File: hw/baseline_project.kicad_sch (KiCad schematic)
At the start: 20 parts, among them J101 EXT_3V3, Q101 IRLD024PBF, SW101 UP, SW102 DOWN, SW103 LEFT, SW104 RIGHT, SW105 MODE, U101 EK-TM4C123GXL, U102 ESP8266-1, U103 Adafruit ST7735R

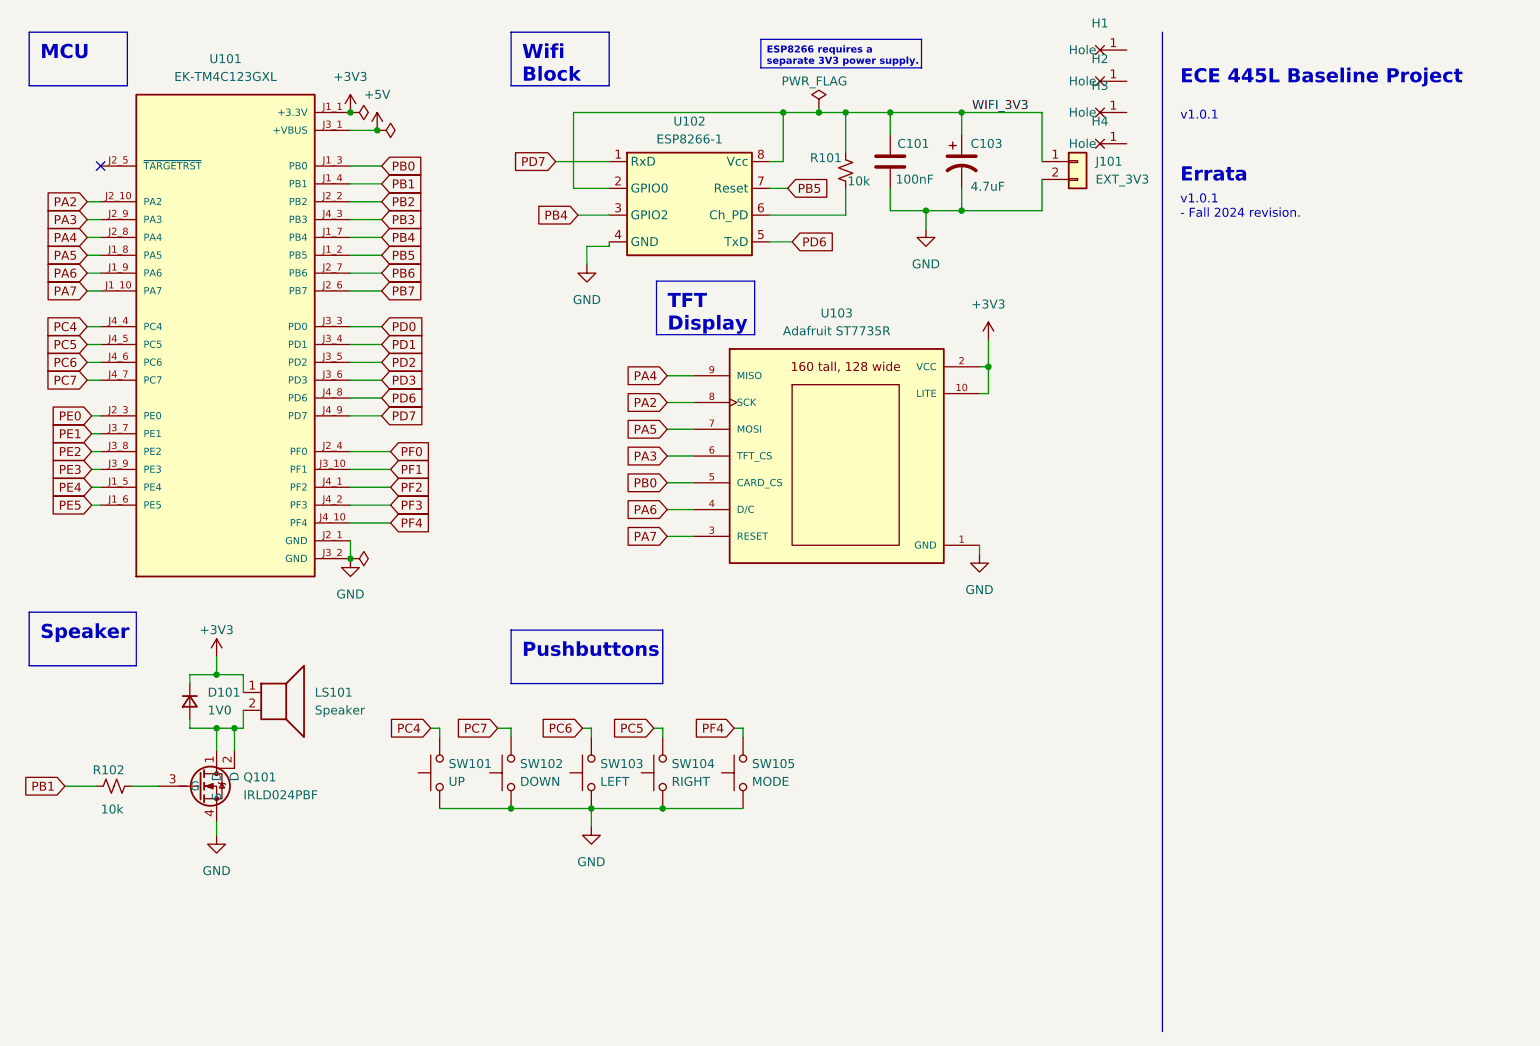
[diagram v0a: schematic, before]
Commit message: changed schematic
Updated schematic pins and layout to make sense with our design for lab3
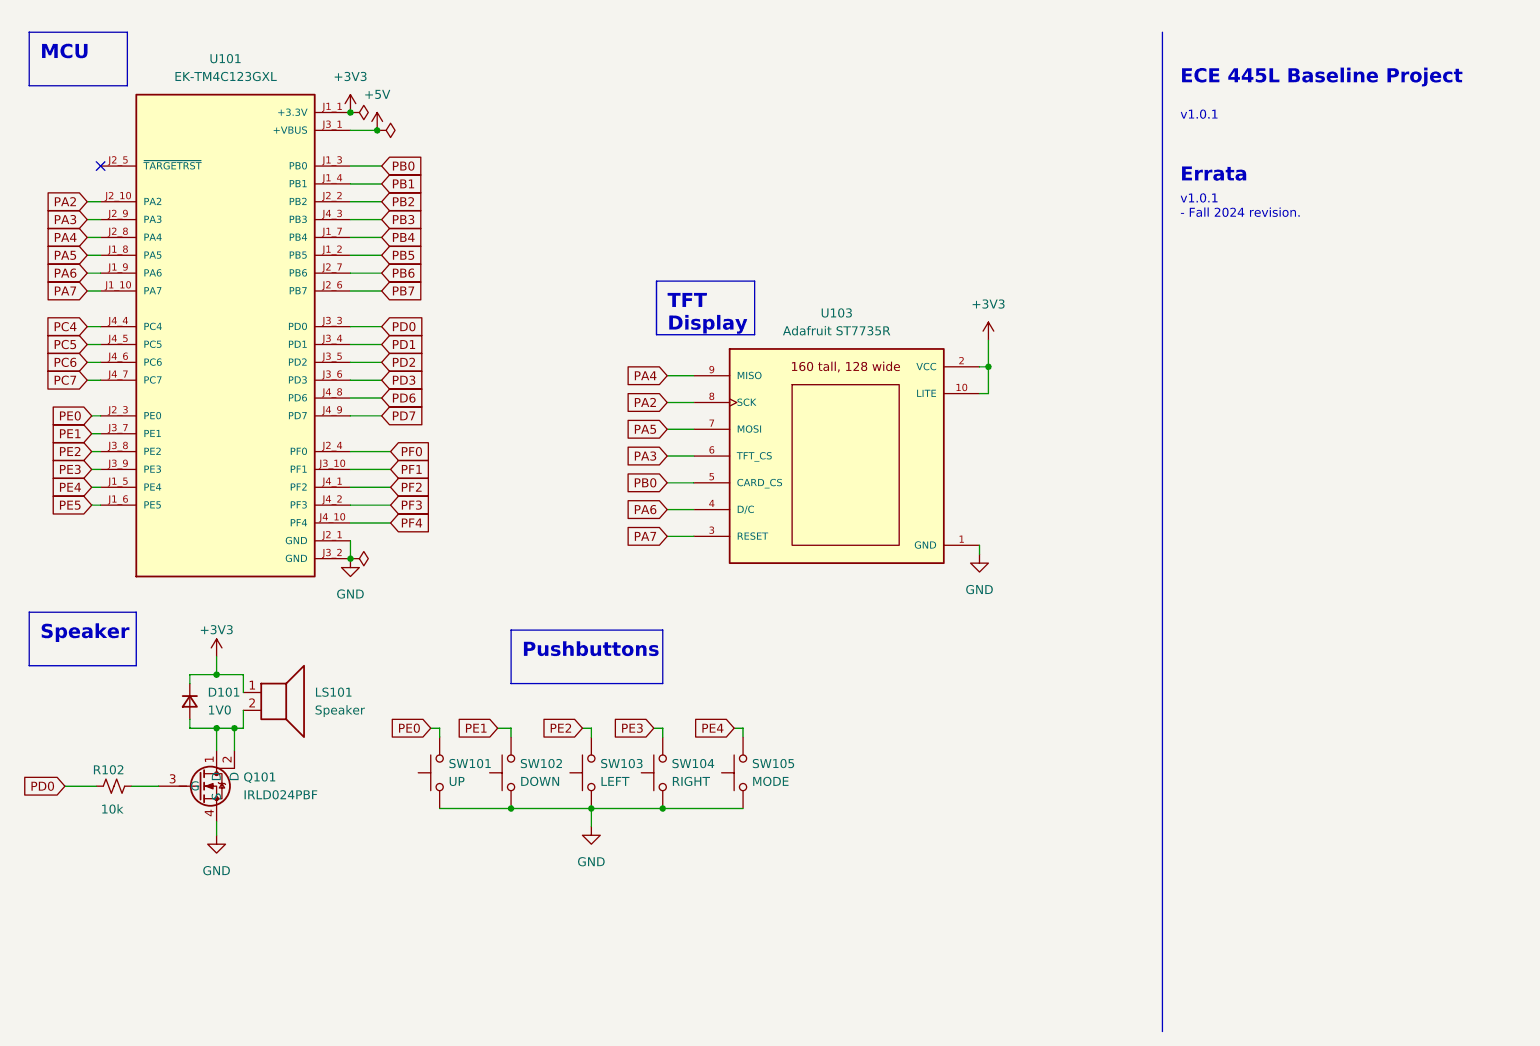
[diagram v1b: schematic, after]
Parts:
- removed C101: 100nF, ECE445L:C_Axial_200mil, symbol ECE445L:C
- removed C103: 4.7uF, ECE445L:CP_Radial_Tantal200mil, symbol ECE445L:C_Polarized
- removed H1, H2, H3, H4: ~, ECE445L:MountingHole_4_40, symbol ECE445L:MountingHole
- removed J101: EXT_3V3, Connector_Samtec_HPM_THT:Samtec_HPM-02-01-x-S_Straight_1x02_Pitch5.08mm, symbol Connector_Generic:Conn_01x02
- removed R101: 10k, ECE445L:R_Axial_DIN0204_L3.6mm_D1.6mm_P7.62mm_Horizontal, symbol ECE445L:R_0.125W
- removed U102: ESP8266-1, ECE445L:PinHeader_2x04_P2.54mm_Vertical, symbol ECE445L:ESP8266-1
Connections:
- net PB1: no longer R102.1
- net PC4: no longer SW101.2
- net PC5: no longer SW104.2
- net PC6: no longer SW103.2
- net PC7: no longer SW102.2
- net PD0: now also R102.1
- net PE0: now also SW101.2
- net PE1: now also SW102.2
- net PE2: now also SW103.2
- net PE3: now also SW104.2
- net PE4: now also SW105.2
- net PF4: no longer SW105.2

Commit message: new updates
added heartbeat back in (untested). Made an initial attempt to draw the background of the clock, probably won't work.
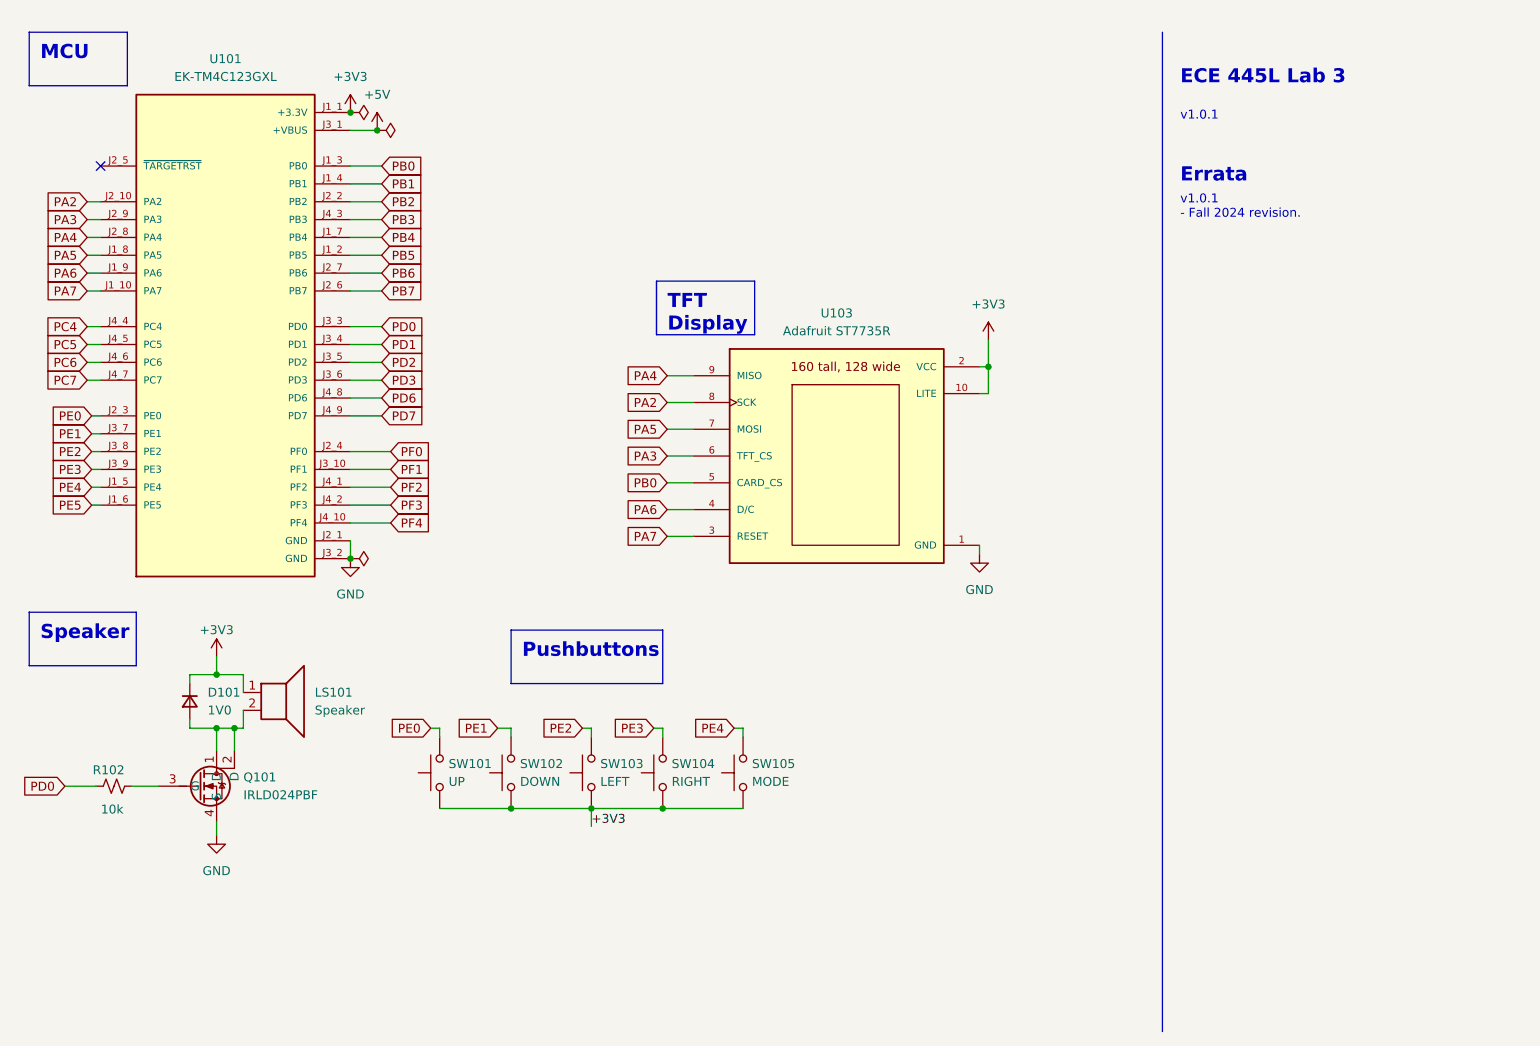
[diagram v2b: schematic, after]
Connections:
- net +3V3: now also SW101.1, SW102.1, SW103.1, SW104.1, SW105.1
- net GND: no longer SW101.1, SW102.1, SW103.1, SW104.1, SW105.1
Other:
- note added: "ECE 445L Lab 3"
- note removed: "ECE 445L Baseline Project"
- title: ECE 445L Baseline Project -> ECE 445L Lab 3
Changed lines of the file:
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@@
 	(paper "A4")
 	(title_block
-		(title "ECE 445L Baseline Project")
+		(title "ECE 445L Lab 3")
 		(date "2024-08-07")
 		(rev "v1.0.1")
@@
 		)
 	)
-	(text "ECE 445L Baseline Project"
+	(text "ECE 445L Lab 3\n"
 		(exclude_from_sim no)
 		(at 179.07 22.86 0)
@@
 				(thickness 0.4)
 				(bold yes)
+			)
+			(justify left bottom)
+		)
+	)
+	(label "+3V3"
+		(at 95.25 128.27 0)
+		(fields_autoplaced yes)
+		(effects
+			(font
+				(size 1.27 1.27)
 			)
 			(justify left bottom)
@@
 					(unit 1)
 				)
-			)
-		)
-	)
-	(symbol
-		(lib_id "power:GND")
-		(at 95.25 128.27 0)
-		(unit 1)
-		(exclude_from_sim no)
-		(in_bom yes)
-		(on_board yes)
-		(dnp no)
-		(fields_autoplaced yes)
-		(property "Reference" "#PWR0107"
-			(at 95.25 134.62 0)
-			(effects
-				(font
-					(size 1.27 1.27)
-				)
-				(hide yes)
-			)
-		)
-		(property "Value" "GND"
-			(at 95.25 133.35 0)
-			(effects
-				(font
-					(size 1.27 1.27)
-				)
-			)
-		)
-		(property "Footprint" ""
-			(at 95.25 128.27 0)
-			(effects
-				(font
-					(size 1.27 1.27)
-				)
-				(hide yes)
-			)
-		)
-		(property "Datasheet" ""
-			(at 95.25 128.27 0)
-			(effects
-				(font
-					(size 1.27 1.27)
-				)
-				(hide yes)
-			)
-		)
-		(property "Description" "Power symbol creates a global label with name \"GND\" , ground"
-			(at 95.25 128.27 0)
-			(effects
-				(font
-					(size 1.27 1.27)
-				)
-				(hide yes)
-			)
-		)
-		(pin "1"
-		)
-		(instances
-			(project "baseline_project"
-				(path "/69b823fd-c065-40ff-9bb9-c5835555f3eb"
-					(reference "#PWR0107")
-					(unit 1)
-				)
